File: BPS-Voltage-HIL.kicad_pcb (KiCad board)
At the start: 2 copper layers, 86 x 58.9 mm, 50 parts, among them J1 Conn_01x02_Socket, J10 Conn_01x02_Pin, J11 Conn_01x02_Pin, J12 Conn_01x02_Pin, J13 Conn_01x02_Pin, J14 Conn_01x02_Pin, J15 Conn_01x02_Pin, J16 Conn_01x02_Pin, J17 Conn_01x02_Pin, J18 Conn_01x02_Pin, J19 Conn_01x02_Pin, J2 Out1_1, J20 Conn_01x02_Pin, J21 Conn_01x02_Pin, J22 Conn_01x02_Pin, J23 Conn_01x02_Pin, J24 Conn_01x02_Pin, J25 Conn_01x02_Pin, J26 Conn_01x02_Pin, J27 Conn_01x02_Pin, J28 Conn_01x02_Pin, J29 Conn_01x02_Pin, J3 SOMConnector, J30 Conn_01x02_Pin, J31 Conn_01x02_Pin, J32 Conn_01x02_Pin, J33 Conn_01x02_Pin, J34 Conn_01x02_Pin, J35 Conn_01x02_Pin, J36 Conn_01x02_Pin, J37 Conn_01x02_Pin, J38 Conn_01x02_Pin, J4 Out1_2, J5 Out2_1, J6 Out2_2, J7 Conn_01x02_Pin, J8 Conn_01x02_Pin, J9 Conn_01x02_Pin, U1 DAC7311xDCK, U2 DAC7311xDCK, U3 DAC7311xDCK, U4 DAC7311xDCK

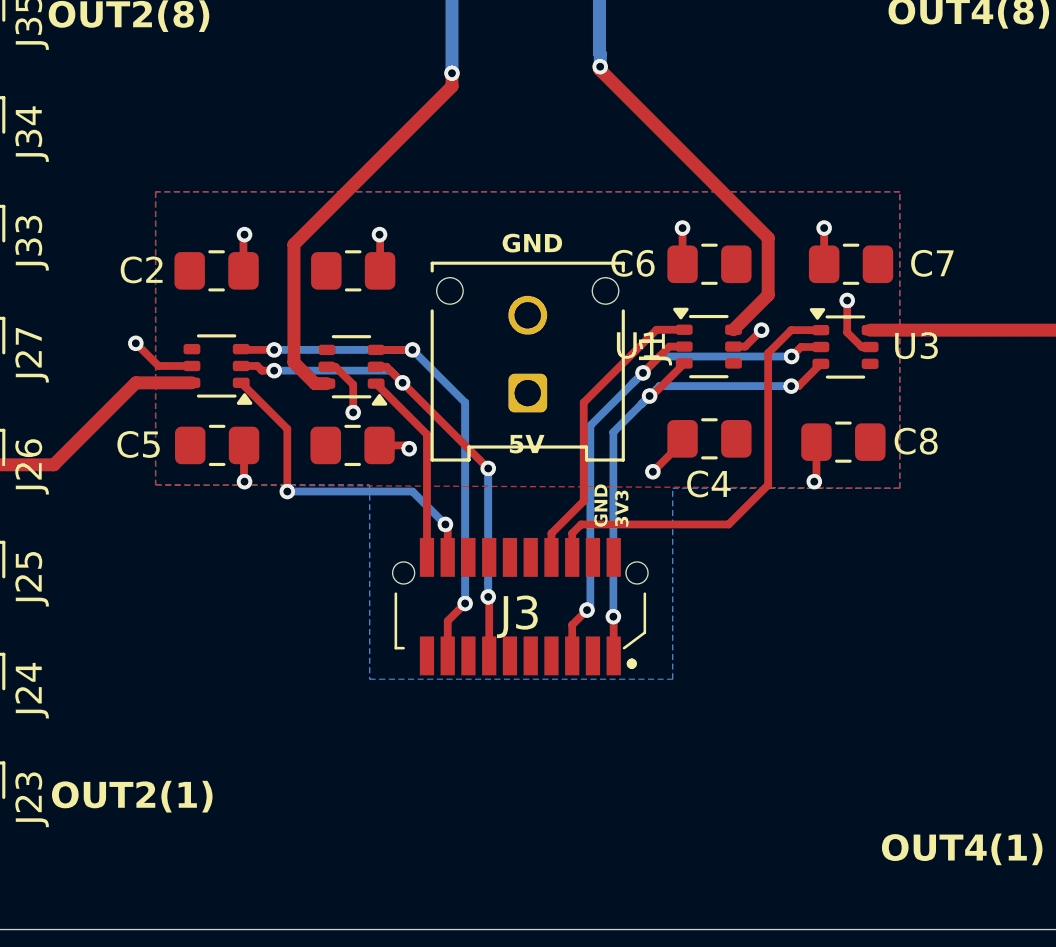
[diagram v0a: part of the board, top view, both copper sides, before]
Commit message: psom connector footprint is not right
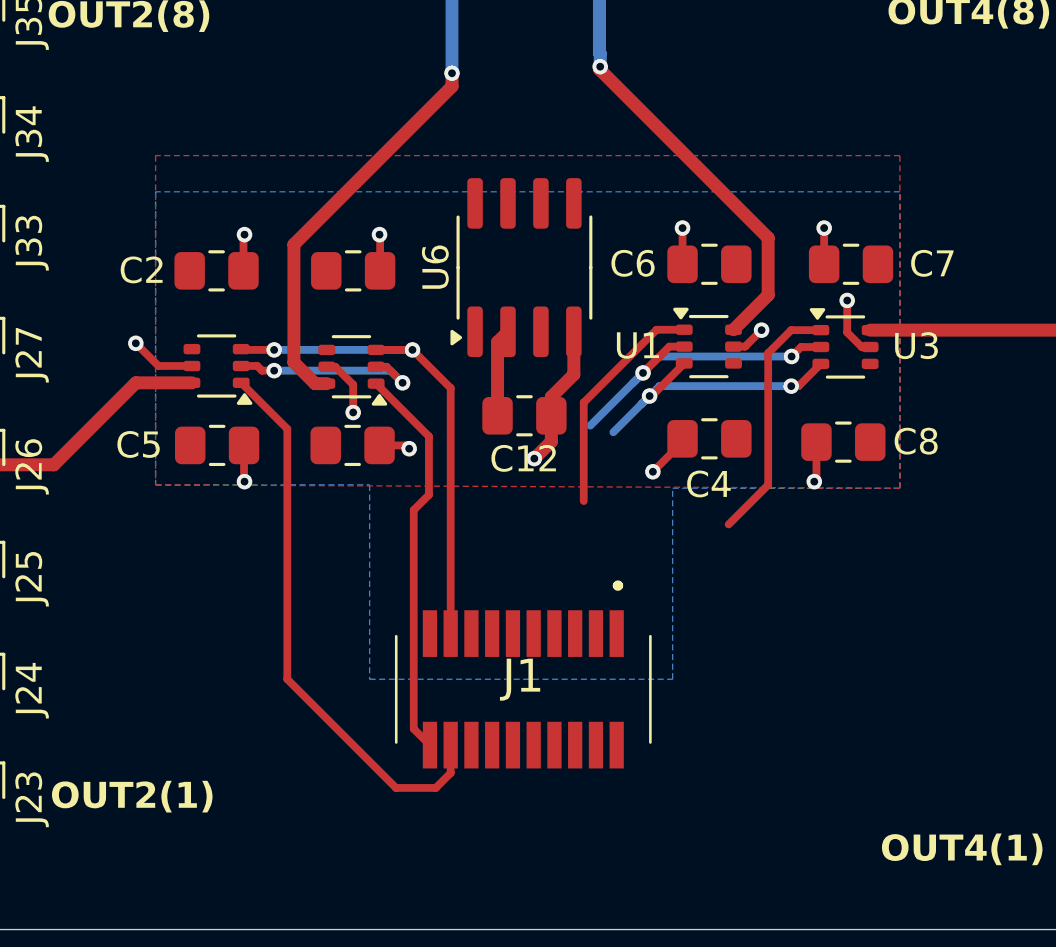
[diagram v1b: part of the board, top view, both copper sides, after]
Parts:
- removed J3: SOMConnector, UTSVT_Connectors:Molex_52465-2070
- added C12: 0.1u, Capacitor_SMD:C_0805_2012Metric_Pad1.18x1.45mm_HandSolder, F.Cu at (121.9, 82.3)
- added U6: REF02AU, Package_SO:SOIC-8_3.9x4.9mm_P1.27mm, F.Cu at (121.9, 76.6)
- J1: value Conn_01x02_Socket -> SOMConnector; footprint Connector_Molex:Molex_Micro-Fit_3.0_43045-0212_2x01_P3.00mm_Vertical -> UTSVT_Connectors:Molex_53307-2071
- moved J1 11.4 mm to (121.9, 92.8), turned to 0 degrees
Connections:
- J1 pad 1: +5V -> /SPI2_MOSI
- J1 pad 2: GND -> unconnected-(J1-Pin_2-Pad2)
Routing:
- net /SPI1_SCK: track 19.7 -> 7.79 mm, vias 4 -> 2
- net /SPI2_SCK: track 21.9 -> 12.7 mm, vias 3 -> 2
- net /CS2: track 12.9 -> 21.5 mm, vias 2 -> 0
- net /SPI2_MOSI: track 20.0 -> 11.4 mm, vias 3 -> 2
- net /CS1: track 7.51 -> 15.3 mm
- net /CS4: track 16.7 -> 9.64 mm
- net GND: track 20.1 -> 25.6 mm, vias 12 -> 13
- net /PSOM_12V: track 0.00 -> 3.41 mm
- net /CS3: track 11.5 -> 8.84 mm
- net /SPI1_MOSI: track 20.9 -> 19.6 mm, vias 3 -> 2
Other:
- board text removed: "5V"
- board text removed: "GND"
- board text removed: "GND 3V3"
